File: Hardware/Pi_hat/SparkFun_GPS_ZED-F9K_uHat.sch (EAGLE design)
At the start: 38 parts, among them J4 U.FL, J7 RASPBERRYPI-40-PIN-GPIO_PTH_N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, U1 UBLOX_ZED_F9K, U3 TRIPLE_BUFFER_74LVC3G07

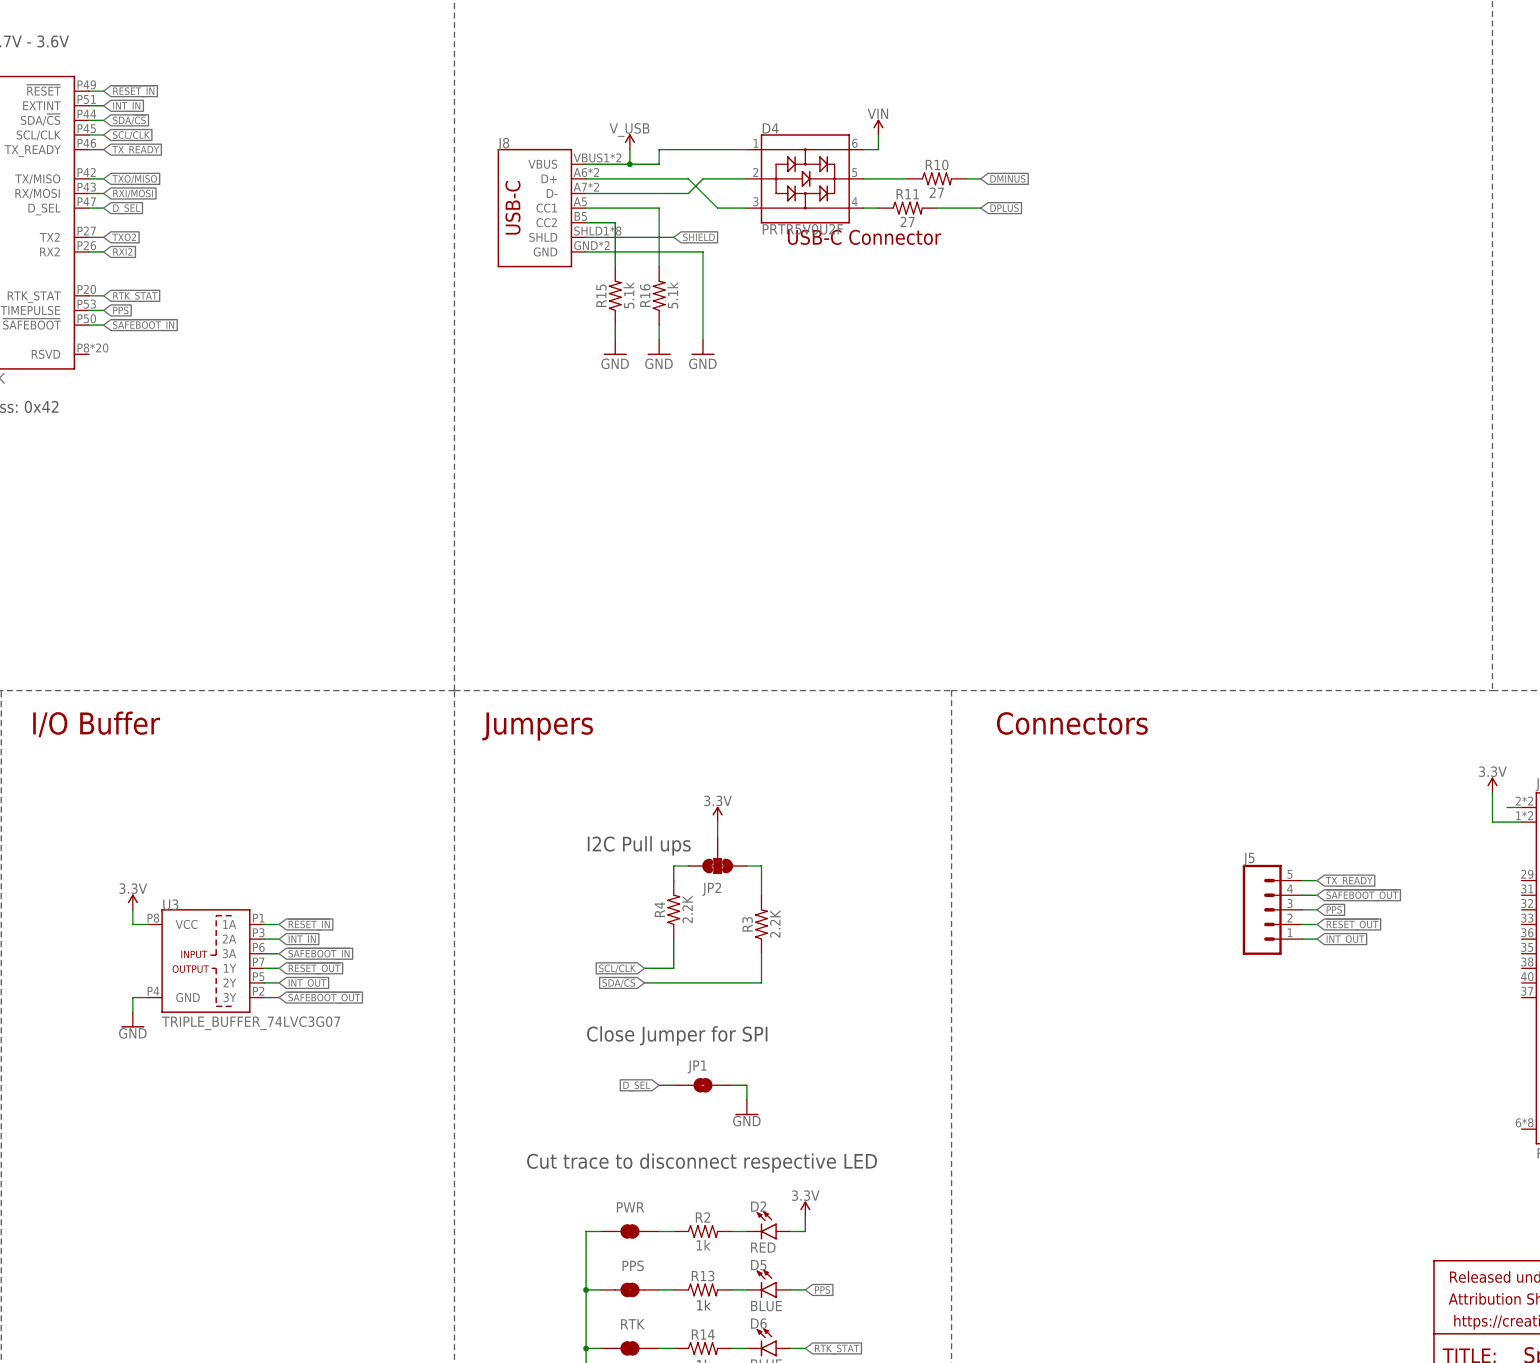
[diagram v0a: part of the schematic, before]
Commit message: Adds trace work for piHat version - still needs silk
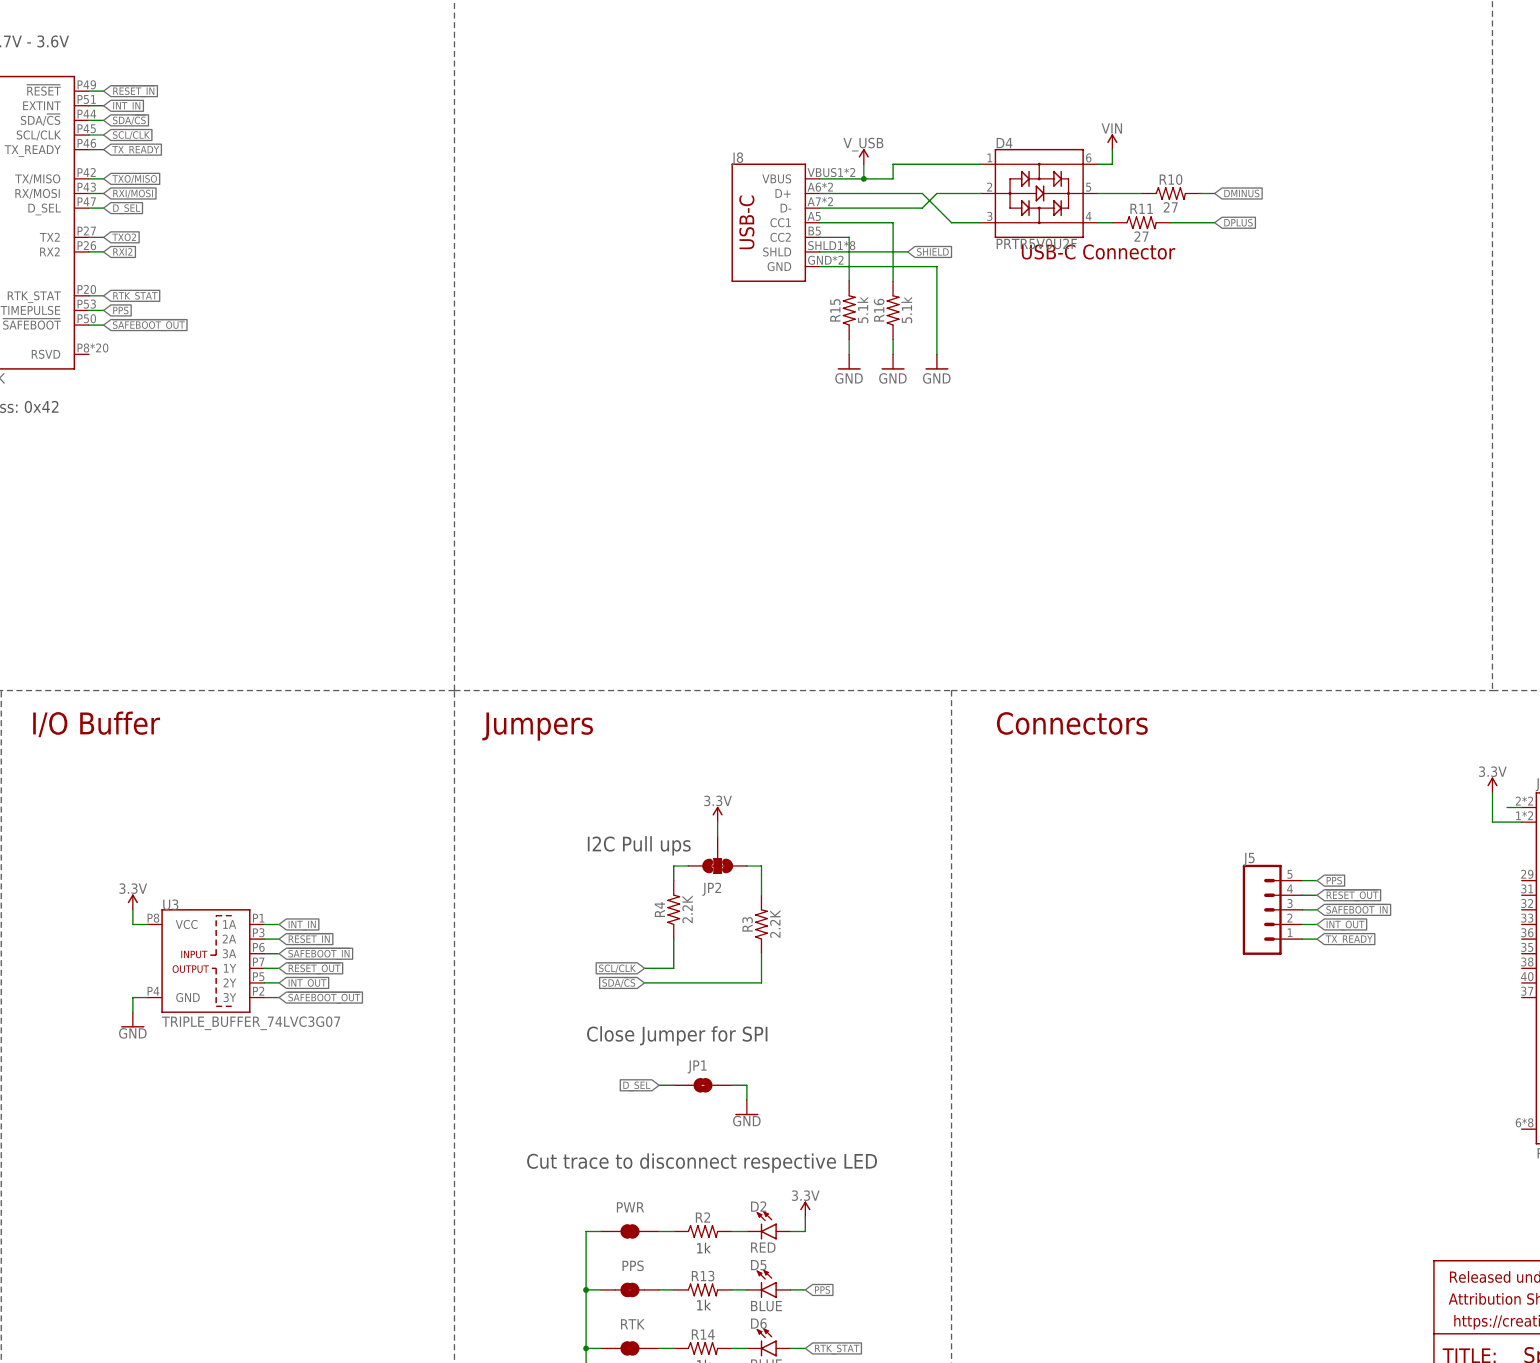
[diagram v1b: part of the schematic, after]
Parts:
- R2: value 1k -> 1KOHM-0402-1/16W-1%; device SparkFun-Resistors:1KOHM-0603-1/10W-1% -> SparkFun-Resistors:1KOHM-0402-1/16W-1%
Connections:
- net !RESET_IN: now also U3.2A; no longer U3.1A
- net !RESET_OUT: now also J5.4; no longer J5.2
- net !SAFEBOOT_IN: now also J5.3; no longer U1.!SAFEBOOT!
- net !SAFEBOOT_OUT: now also U1.!SAFEBOOT!; no longer J5.4
- net INT_IN: now also U3.1A; no longer U3.2A
- net INT_OUT: now also J5.2; no longer J5.1
- net PPS: now also J5.5; no longer J5.3
- net TX_READY: now also J5.1; no longer J5.5
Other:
- moved on the sheet: D4, J8, R10, R11, R15, R16
